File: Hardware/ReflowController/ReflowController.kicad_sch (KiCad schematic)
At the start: 10 parts, among them J1 2060-1452, J10 2060-1452, J11 2060-1452, J12 2060-1452, J4 Conn_01x03_Socket, J5 2060-1452, J6 2060-1452, J7 2060-1452, J8 2060-1452, J9 2060-1452

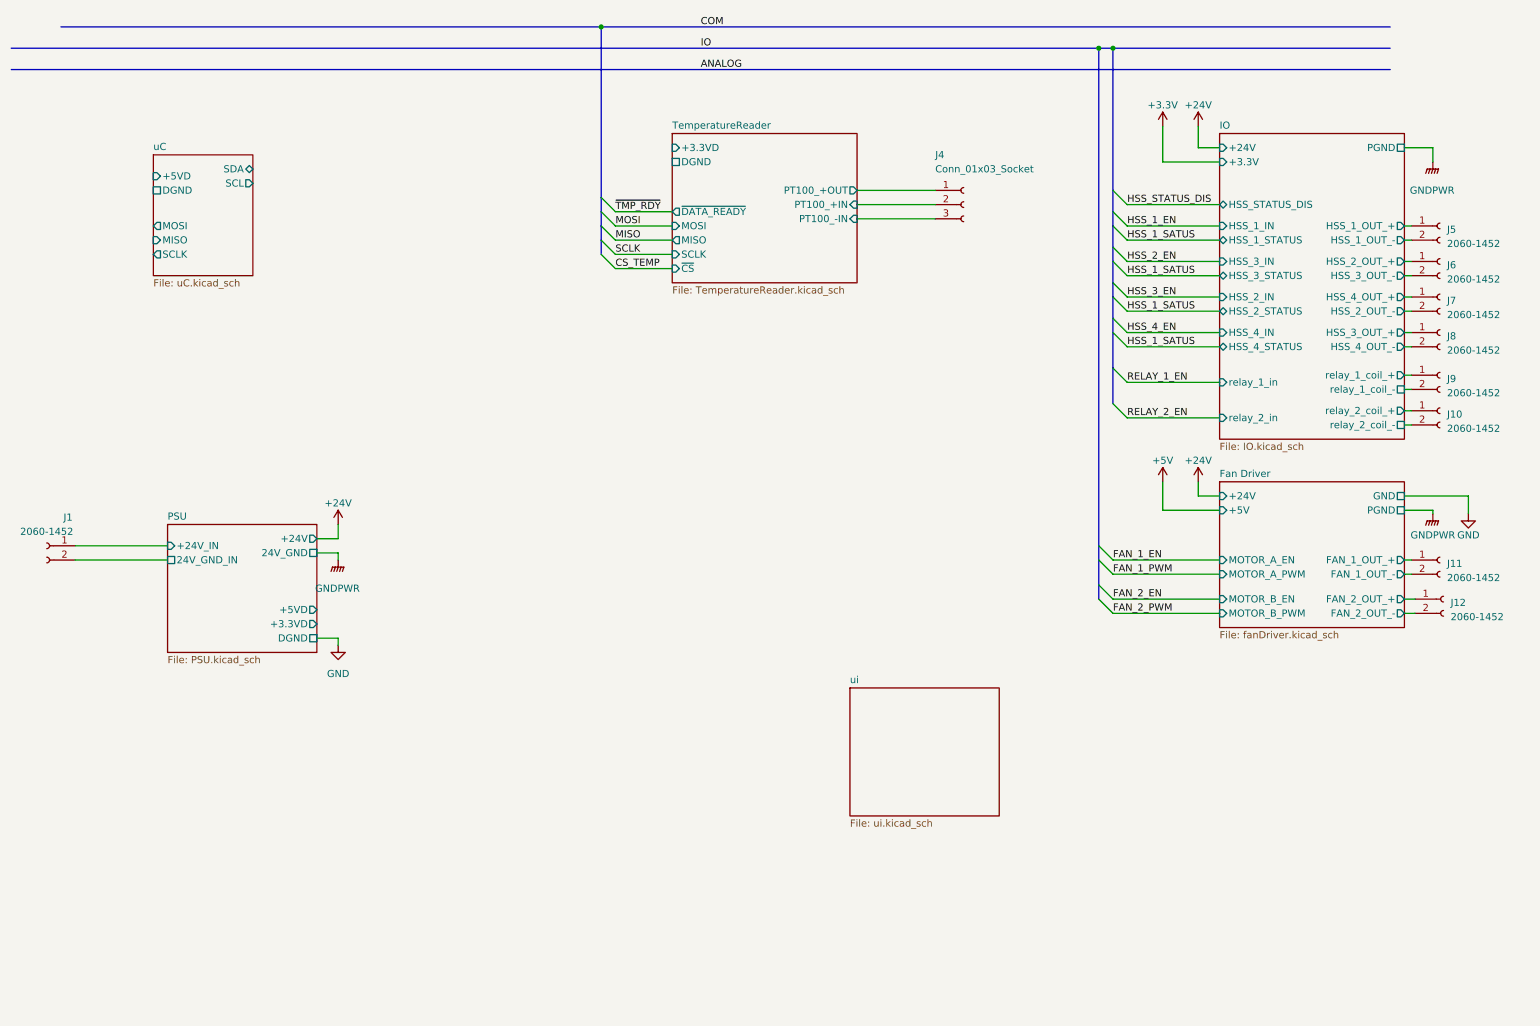
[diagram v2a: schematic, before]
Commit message: Main Schematic rooting and PSU Dqsing ongoing
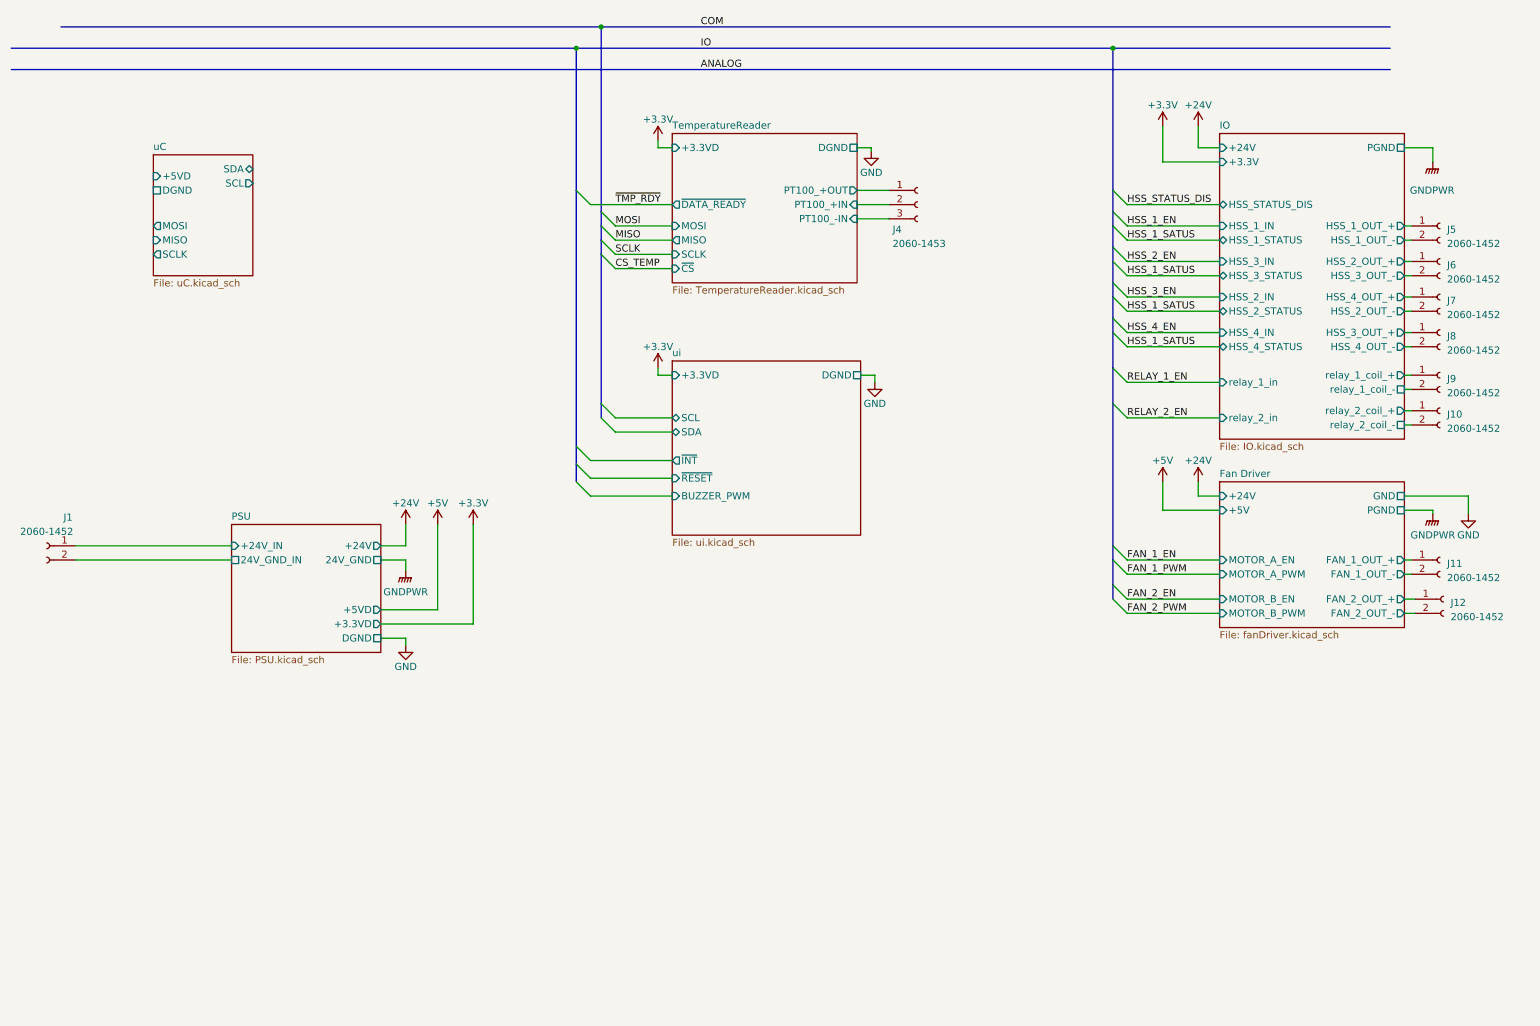
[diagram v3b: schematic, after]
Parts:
- J4: value Conn_01x03_Socket -> 2060-1453
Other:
- sheet ui ports: added +3.3VD, BUZZER_PWM, DGND, SCL, SDA, ~{INT}, ~{RESET}; removed none
- moved on the sheet: J4

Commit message: Finished the desing of the PSUand started with the PCB TODO: missing fuse find a solution
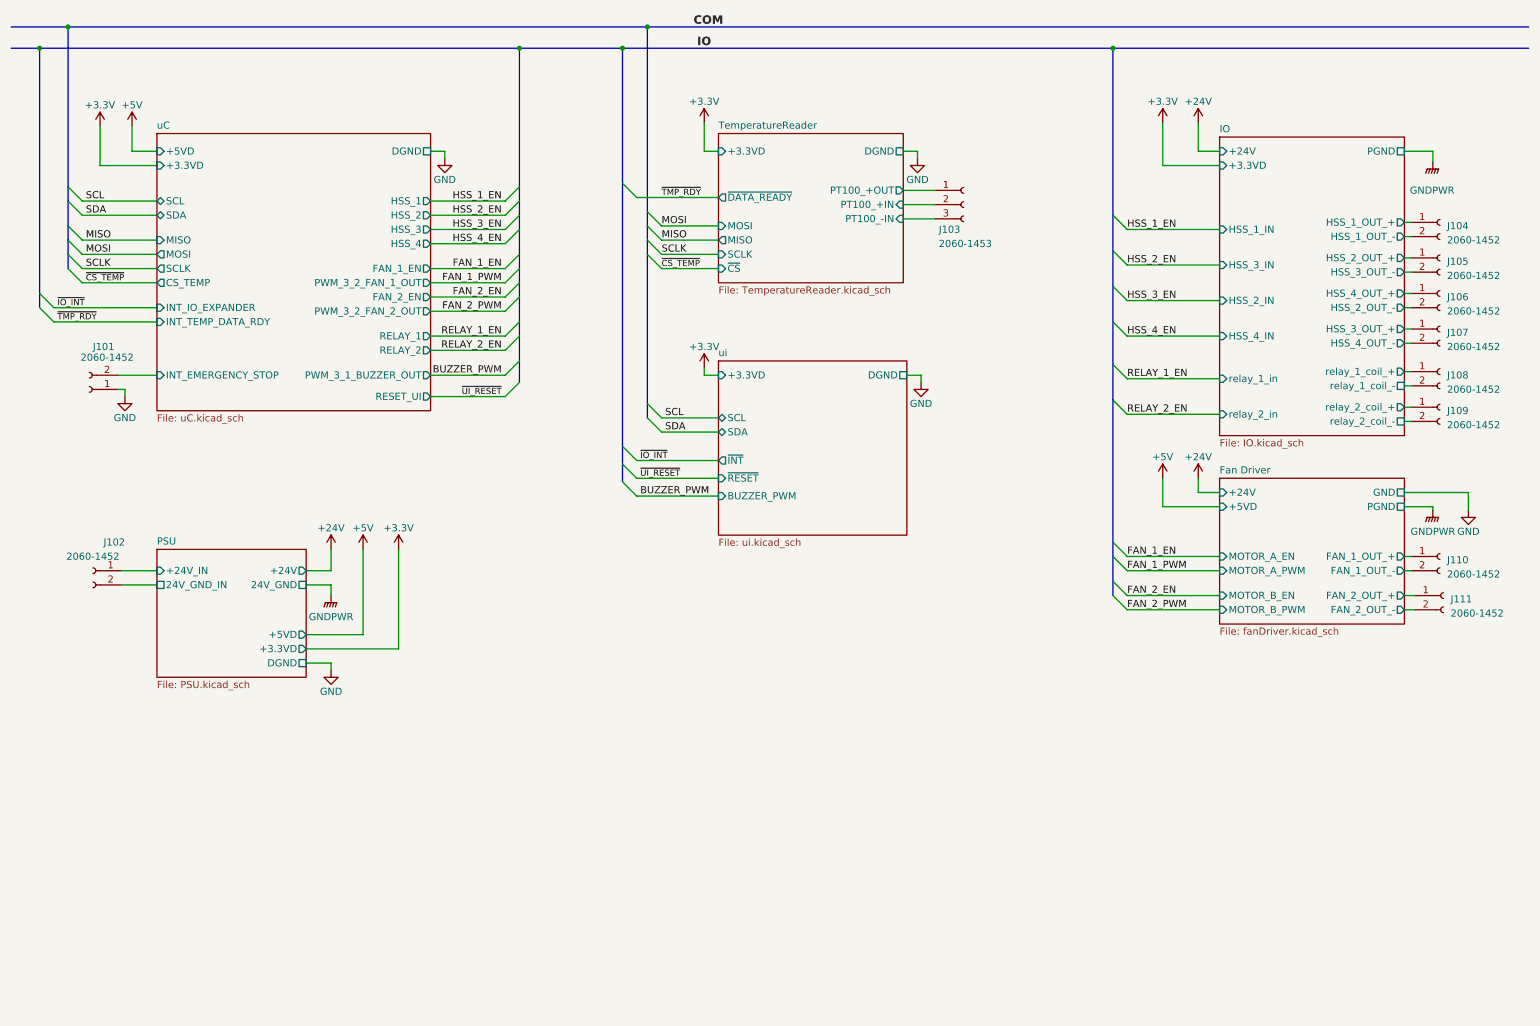
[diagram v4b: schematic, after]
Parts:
- added J101: 2060-1452, 810_connectors_clable_to_Board:wago_2060-1452, symbol Connector:Conn_01x02_Socket
- renumbered J1 to J102, J4 to J103, J5 to J104, J6 to J105, J7 to J106, J8 to J107, J9 to J108, J10 to J109, J11 to J110, J12 to J111
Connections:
- net GND: now also J101.1 (Pin_1)
- new net uC/INT_EMERGENCY_STOP: J101.2 (Pin_2)
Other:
- sheet Fan Driver ports: added +5VD; removed +5V
- sheet IO ports: added +3.3VD; removed +3.3V, HSS_1_STATUS, HSS_2_STATUS, HSS_3_STATUS, HSS_4_STATUS, HSS_STATUS_DIS
- sheet uC ports: added +3.3VD, CS_TEMP, FAN_1_EN, FAN_2_EN, HSS_1, HSS_2, HSS_3, HSS_4, INT_EMERGENCY_STOP, INT_IO_EXPANDER, INT_TEMP_DATA_RDY, PWM_3_1_BUZZER_OUT, PWM_3_2_FAN_1_OUT, PWM_3_2_FAN_2_OUT, RELAY_1, RELAY_2, RESET_UI; removed none
- moved on the sheet: J102, J103, J104, J105, J106, J107, J108, J109, J110, J111
